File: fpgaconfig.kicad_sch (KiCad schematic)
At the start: 20 parts, among them J1 SPI Header, U1 ICE40UP5K-SG48ITR, U9 W25Q32JVSS

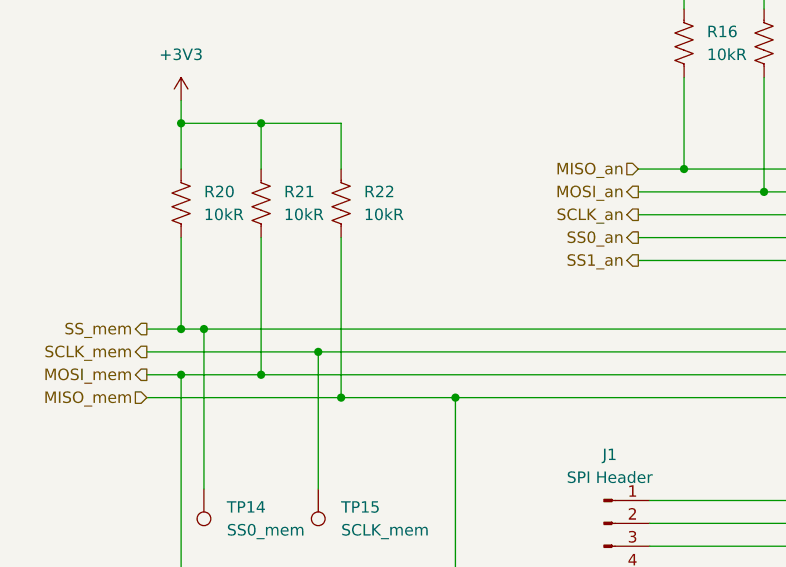
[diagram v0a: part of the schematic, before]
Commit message: Fix review suggestions from non-fpga board
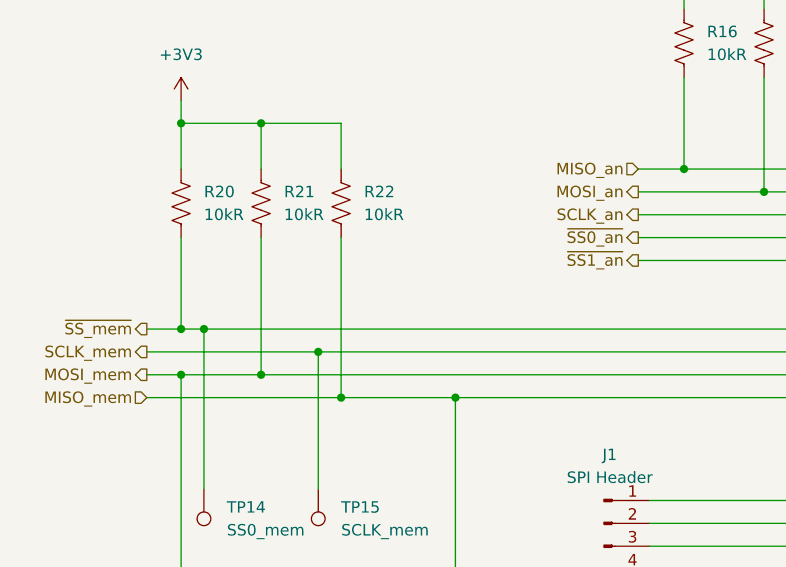
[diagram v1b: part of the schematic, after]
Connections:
- net SS0_an renamed ~{SS0_an}
- net SS1_an renamed ~{SS1_an}
- net SS_mem renamed ~{SS_mem}
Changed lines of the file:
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@@
 		)
 	)
-	(hierarchical_label "SS_mem"
+	(hierarchical_label "~{SS_mem}"
 		(shape output)
 		(at 35.56 77.47 180)
@@
 		)
 	)
-	(hierarchical_label "SS0_an"
+	(hierarchical_label "~{SS0_an}"
 		(shape output)
 		(at 90.17 67.31 180)
@@
 		)
 	)
-	(hierarchical_label "SS1_an"
+	(hierarchical_label "~{SS1_an}"
 		(shape output)
 		(at 90.17 69.85 180)
